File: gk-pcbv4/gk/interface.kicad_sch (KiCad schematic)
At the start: 26 parts, among them J11 Conn_01x20, U14 TPS2051BDBV, U15 LSM6DSL, U18 LIS2MDL

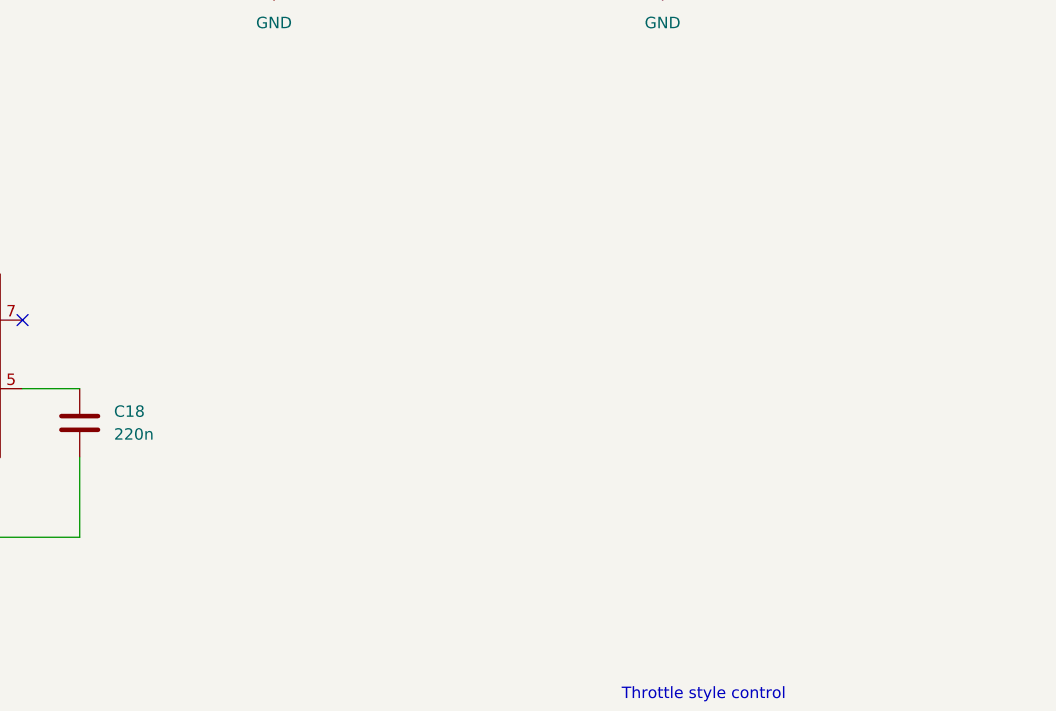
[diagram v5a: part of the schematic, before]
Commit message: move LB/RB to main board
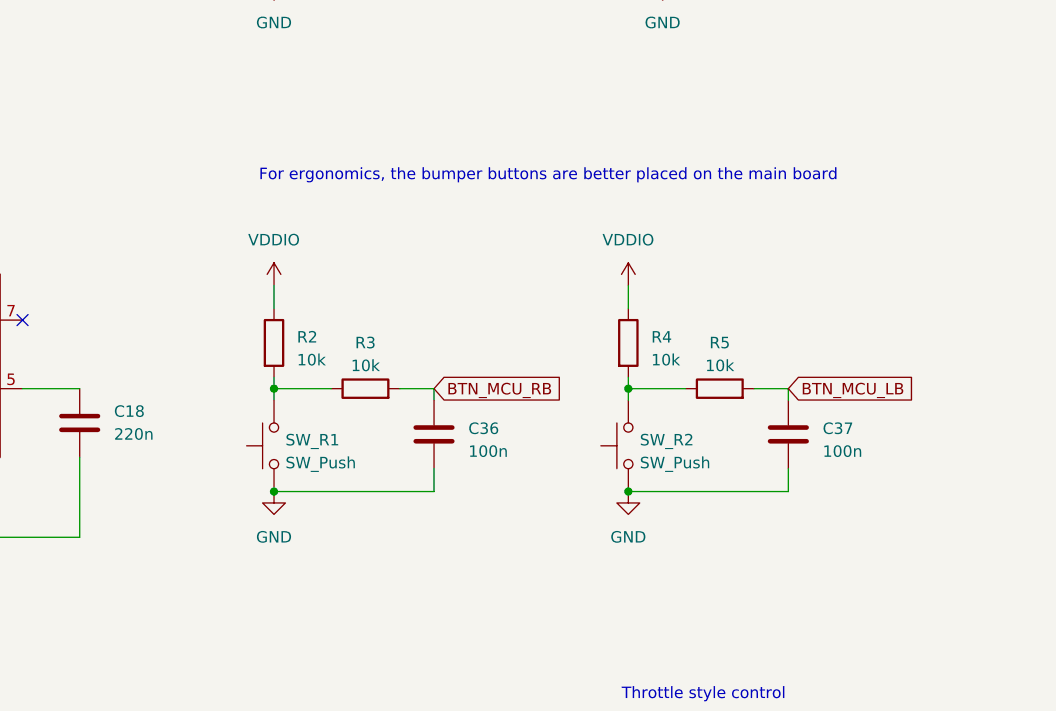
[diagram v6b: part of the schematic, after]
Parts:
- added C36, C37: 100n, Capacitor_SMD:C_0603_1608Metric, symbol Device:C
- added R2, R3, R4, R5: 10k, Resistor_SMD:R_0603_1608Metric, symbol Device:R
- added SW_R1, SW_R2: SW_Push, gk:TouchButton-8x8mm_2, symbol Switch:SW_Push
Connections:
- net GND: now also C36.2, C37.2, SW_R1.1, SW_R2.1
- net VDDIO: now also R2.1, R4.1
- new net: R4.2, R5.1, SW_R2.2
- new net: R2.2, R3.1, SW_R1.2
- new net BTN_MCU_LB: C37.1, R5.2
- new net BTN_MCU_RB: C36.1, R3.2
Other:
- note added: "For ergonomics, the bumper buttons are better placed on the main board"

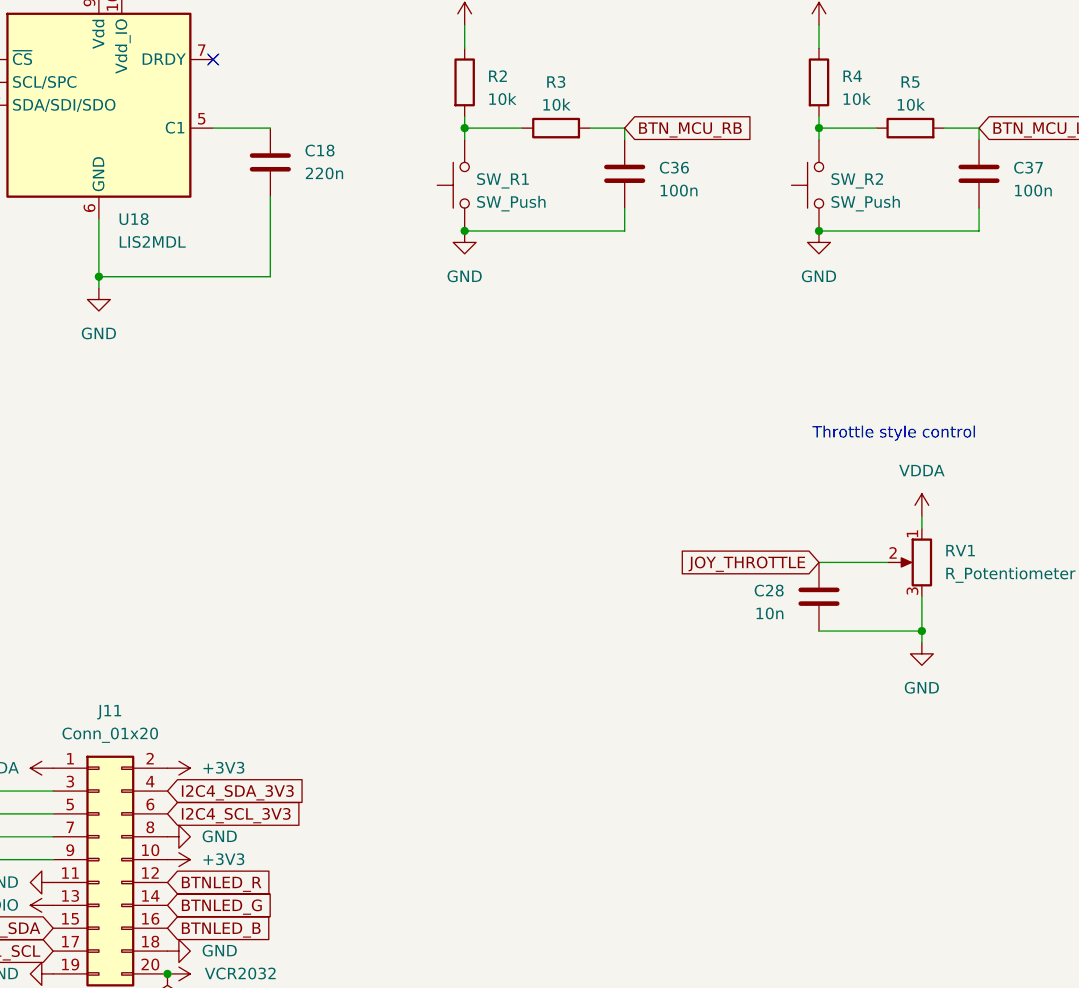
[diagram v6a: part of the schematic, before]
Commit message: update pcb routing based on new v2 changes
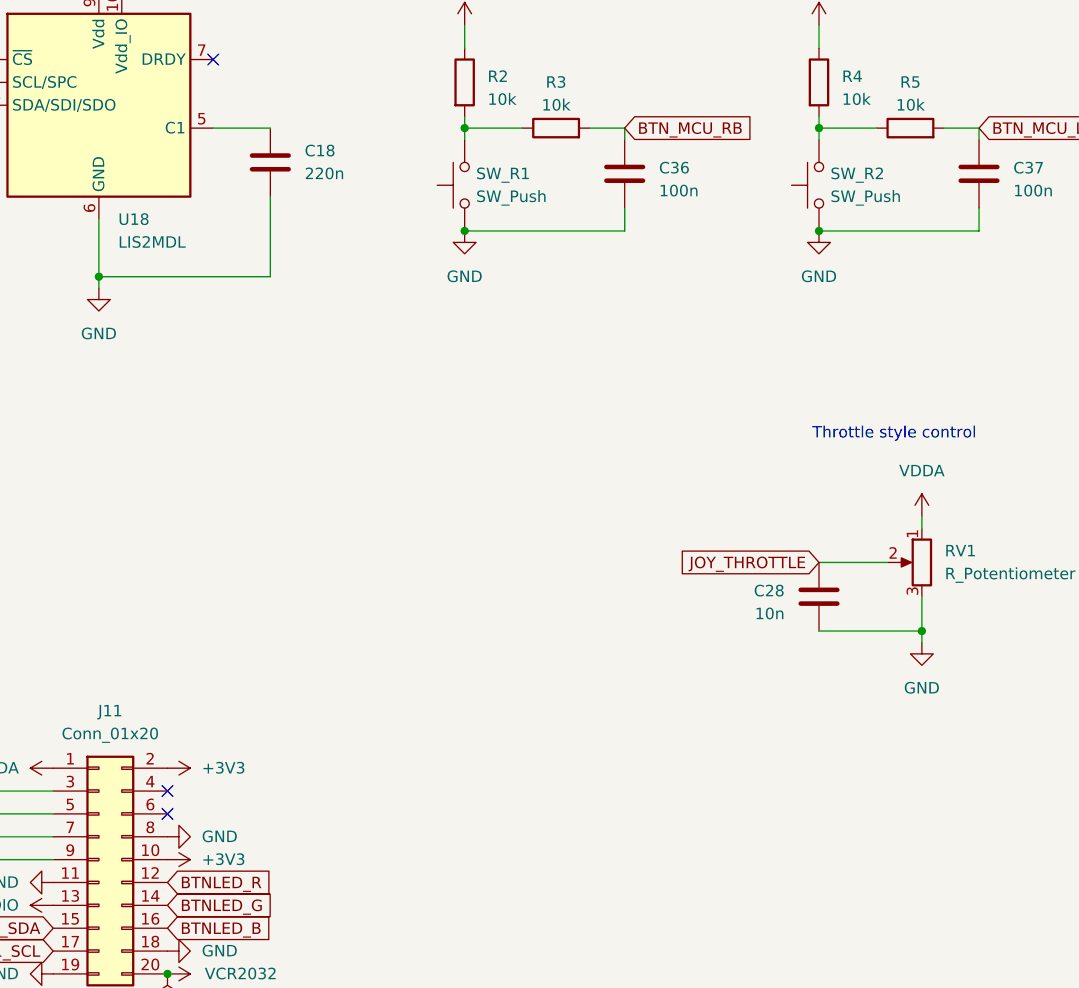
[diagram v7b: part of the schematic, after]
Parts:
- C18: footprint (none) -> Capacitor_SMD:C_0603_1608Metric
- SW_R1, SW_R2: footprint gk:TouchButton-8x8mm_2 -> gk-pcbv3:TouchButton-8x8mm_2
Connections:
- net I2C4_SCL_3V3: no longer names the net of J11.6 (Pin_6)
- net I2C4_SDA_3V3: no longer names the net of J11.4 (Pin_4)
- no-connect marks 4 -> 6
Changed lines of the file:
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@@
 	)
 	(no_connect
+		(at 154.94 170.18)
+	)
+	(no_connect
+		(at 154.94 167.64)
+	)
+	(no_connect
 		(at 101.6 38.1)
 	)
@@
 		)
 	)
-	(global_label "I2C4_SCL_3V3"
-		(shape input)
-		(at 154.94 170.18 0)
-		(fields_autoplaced yes)
-		(effects
-			(font
-				(size 1.27 1.27)
-			)
-			(justify left)
-		)
-		(property "Intersheetrefs" "${INTERSHEET_REFS}"
-			(at 171.1694 170.18 0)
-			(effects
-				(font
-					(size 1.27 1.27)
-				)
-				(justify left)
-				(hide yes)
-			)
-		)
-	)
 	(global_label "JOY_A_X"
 		(shape input)
@@
 		)
 	)
-	(global_label "I2C4_SDA_3V3"
-		(shape input)
-		(at 154.94 167.64 0)
-		(fields_autoplaced yes)
-		(effects
-			(font
-				(size 1.27 1.27)
-			)
-			(justify left)
-		)
-		(property "Intersheetrefs" "${INTERSHEET_REFS}"
-			(at 171.2299 167.64 0)
-			(effects
-				(font
-					(size 1.27 1.27)
-				)
-				(justify left)
-				(hide yes)
-			)
-		)
-	)
 	(global_label "BTN_MCU_LB"
 		(shape input)
@@
 		(fields_autoplaced yes)
 		(property "Reference" "SW_R2"
-			(at 228.6 99.695 90)
+			(at 228.6 99.0599 90)
 			(effects
 				(font
@@
 		)
 		(property "Value" "SW_Push"
-			(at 228.6 102.235 90)
+			(at 228.6 101.5999 90)
 			(effects
 				(font
@@
 			)
 		)
-		(property "Footprint" "gk:TouchButton-8x8mm_2"
+		(property "Footprint" "gk-pcbv3:TouchButton-8x8mm_2"
 			(at 222.25 100.33 0)
 			(effects
@@
 		(fields_autoplaced yes)
 		(property "Reference" "SW_R1"
-			(at 189.23 99.695 90)
+			(at 189.23 99.0599 90)
 			(effects
 				(font
@@
 		)
 		(property "Value" "SW_Push"
-			(at 189.23 102.235 90)
+			(at 189.23 101.5999 90)
 			(effects
 				(font
@@
 			)
 		)
-		(property "Footprint" "gk:TouchButton-8x8mm_2"
+		(property "Footprint" "gk-pcbv3:TouchButton-8x8mm_2"
 			(at 182.88 100.33 0)
 			(effects
@@
 			)
 		)
-		(property "Footprint" ""
+		(property "Footprint" "Capacitor_SMD:C_0603_1608Metric"
 			(at 167.3352 101.6 0)
 			(effects
